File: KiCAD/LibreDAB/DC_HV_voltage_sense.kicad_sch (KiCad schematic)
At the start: 17 parts, among them U401 AMC1311BDWVR, U402 MCP6486UT-E/LT

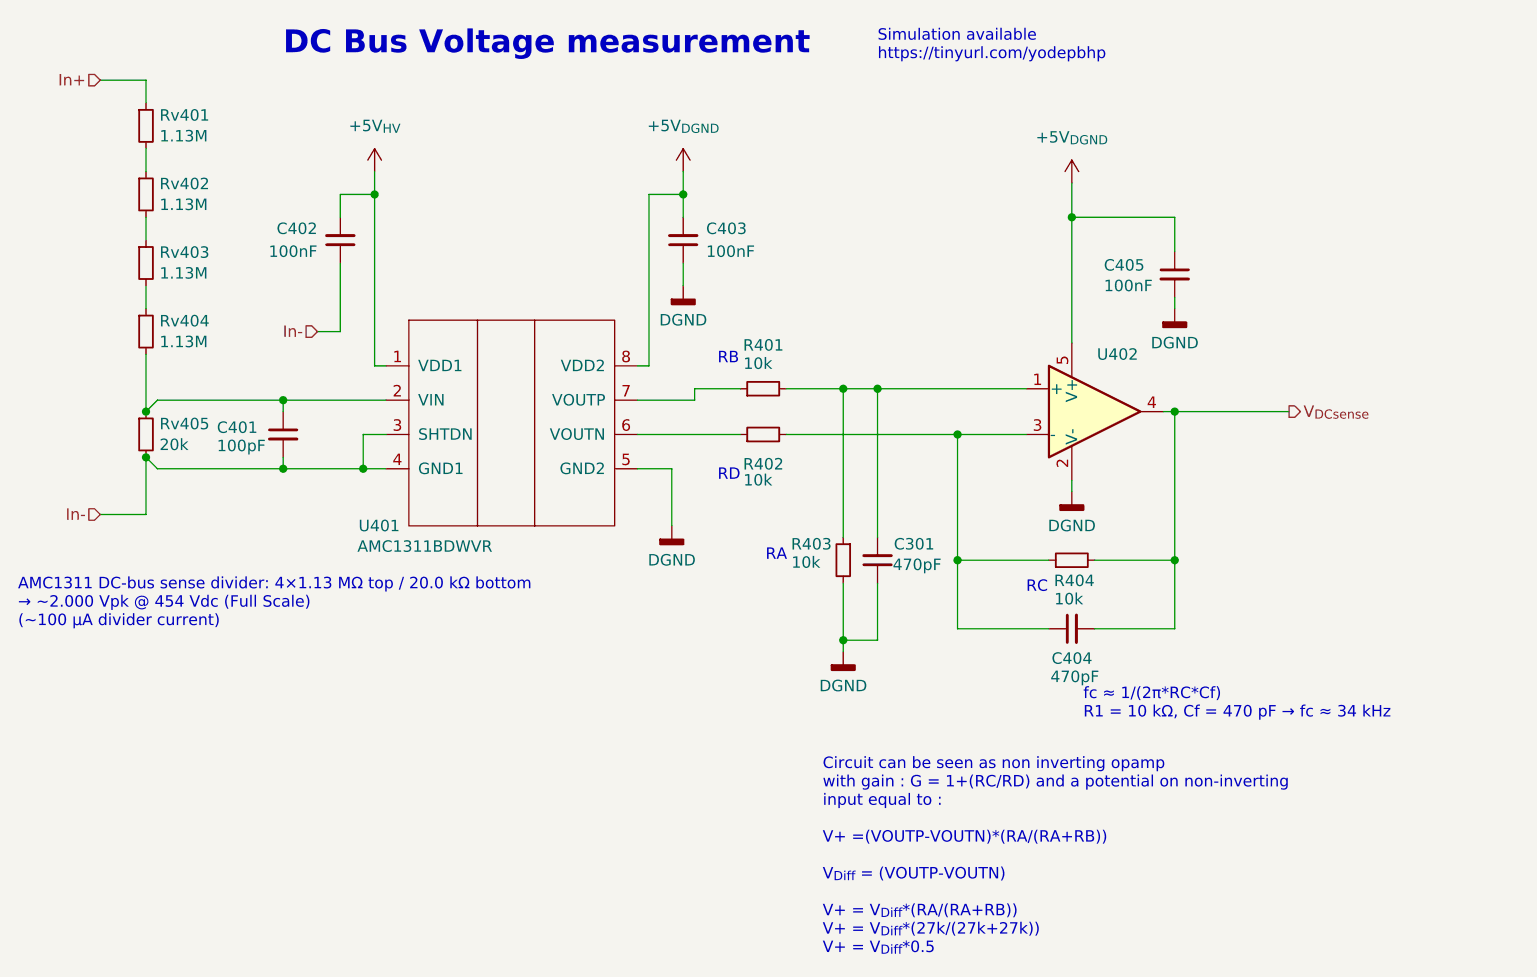
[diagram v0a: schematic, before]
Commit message: Initial kicad schematic draft
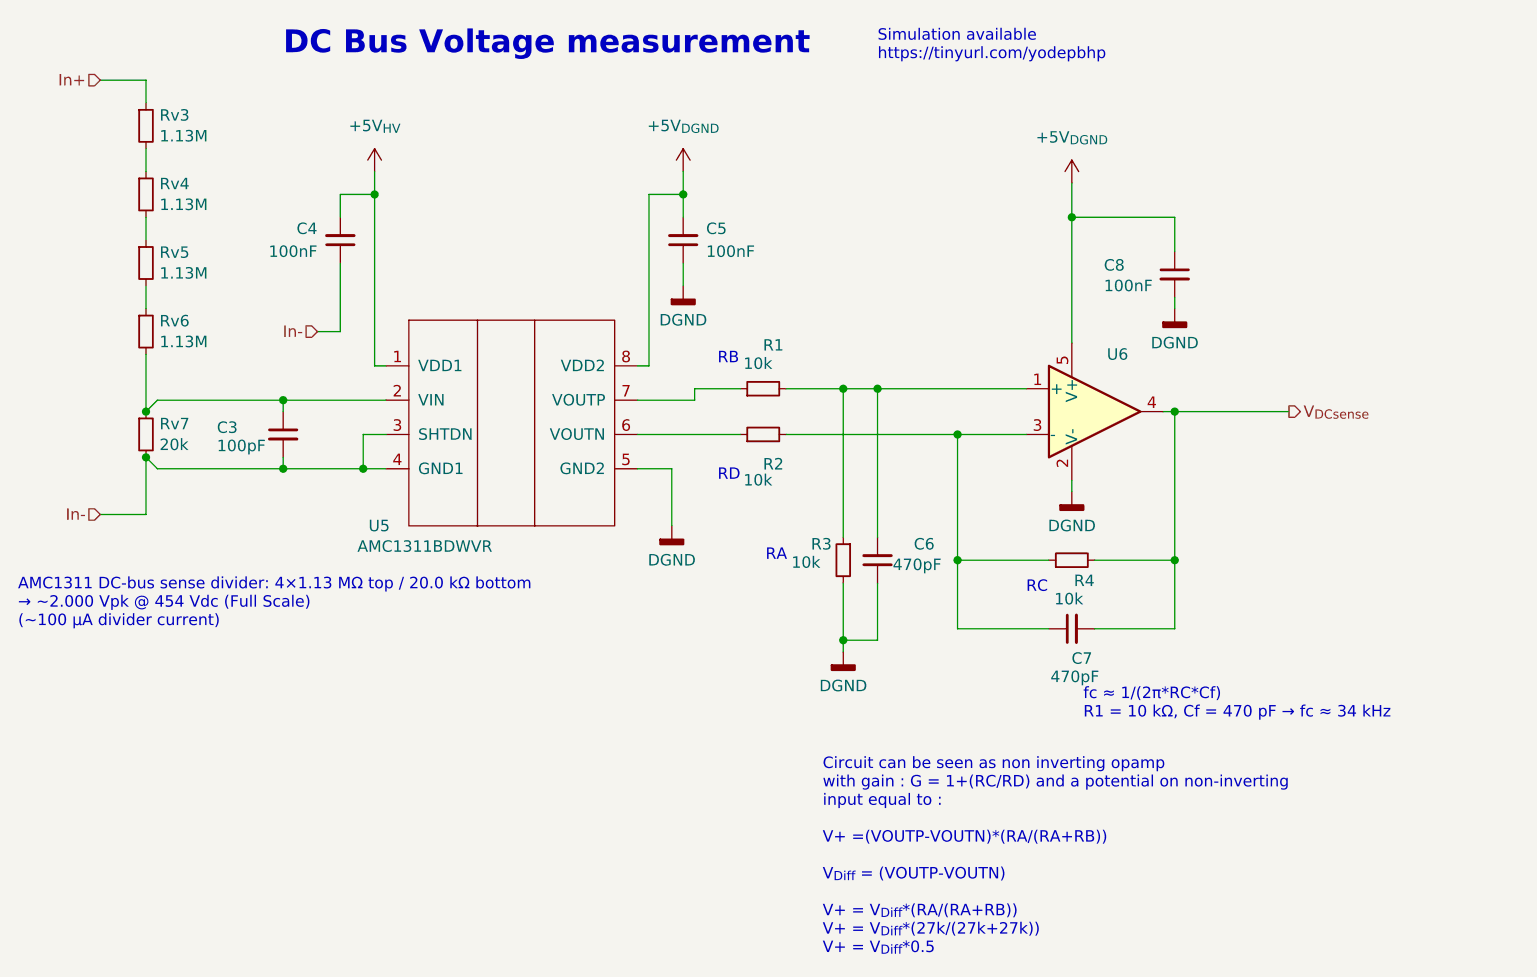
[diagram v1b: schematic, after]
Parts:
- renumbered C401 to C3, C402 to C4, C403 to C5, C301 to C6, C404 to C7, C405 to C8, R401 to R1, R402 to R2, R403 to R3, R404 to R4, Rv401 to Rv3, Rv402 to Rv4, Rv403 to Rv5, Rv404 to Rv6, Rv405 to Rv7, U401 to U5, U402 to U6
